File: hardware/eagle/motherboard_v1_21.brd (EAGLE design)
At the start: 93.6 x 48.3 mm, 43 parts, among them U1 DG412DJZ, Y1 16MHz

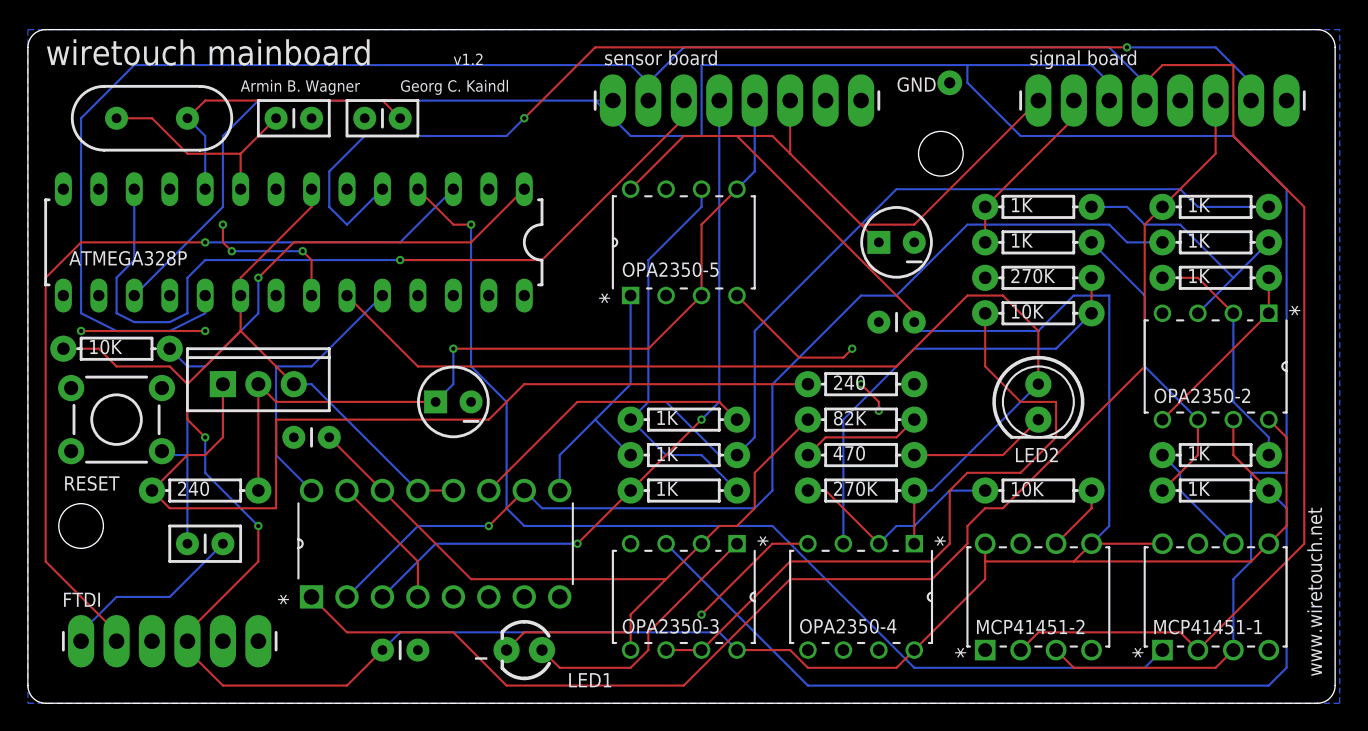
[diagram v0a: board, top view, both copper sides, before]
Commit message: The motherboard version 1.21 includes the missing connection on the OPA2350-5. I also worked a bit on the routing and added a printout of the schematics.
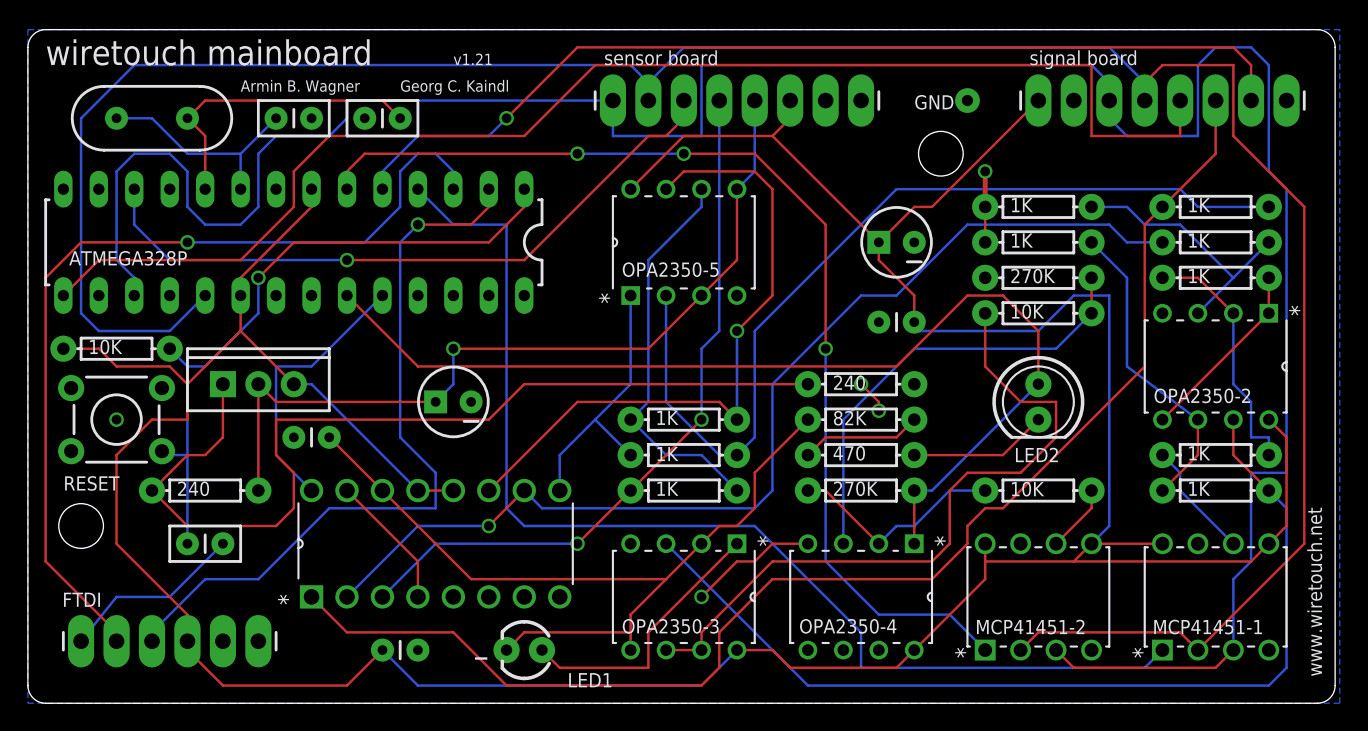
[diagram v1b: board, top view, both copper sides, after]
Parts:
- renumbered U1 to SWITCH
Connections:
- net N$27: now also OPA2350-5.7
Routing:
- net SHIFT_LATCH: track 0.00 -> 96.0 mm
- net N$15: track 0.00 -> 76.4 mm, vias 0 -> 3
- net N$22: track 0.00 -> 53.4 mm, vias 0 -> 1
- net GND: track 73.3 -> 35.1 mm, vias 10 -> 5
- net N$27: track 20.9 -> 47.2 mm, vias 0 -> 1
- net SHIFT_SER: track 163.7 -> 179.3 mm
- net 5V: track 269.8 -> 259.0 mm, vias 2 -> 1
- net N$127: track 58.9 -> 48.4 mm
- net SIG_DIG: track 80.0 -> 70.2 mm, vias 2 -> 1
- net N$25: track 57.6 -> 65.3 mm
- net N$21: track 60.0 -> 64.3 mm
- net N$28: track 78.5 -> 81.5 mm, vias 1 -> 0
- net N$3: track 65.4 -> 68.2 mm
- net SIG_REF: track 93.7 -> 95.2 mm
- net N$12: track 49.0 -> 49.7 mm
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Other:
- board text added: "v1.21"
- board text removed: "v1.2"
